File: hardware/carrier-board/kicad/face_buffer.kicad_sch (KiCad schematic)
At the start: 8 parts, among them J2 HUB75, U1 74AHCT245, U2 74AHCT245

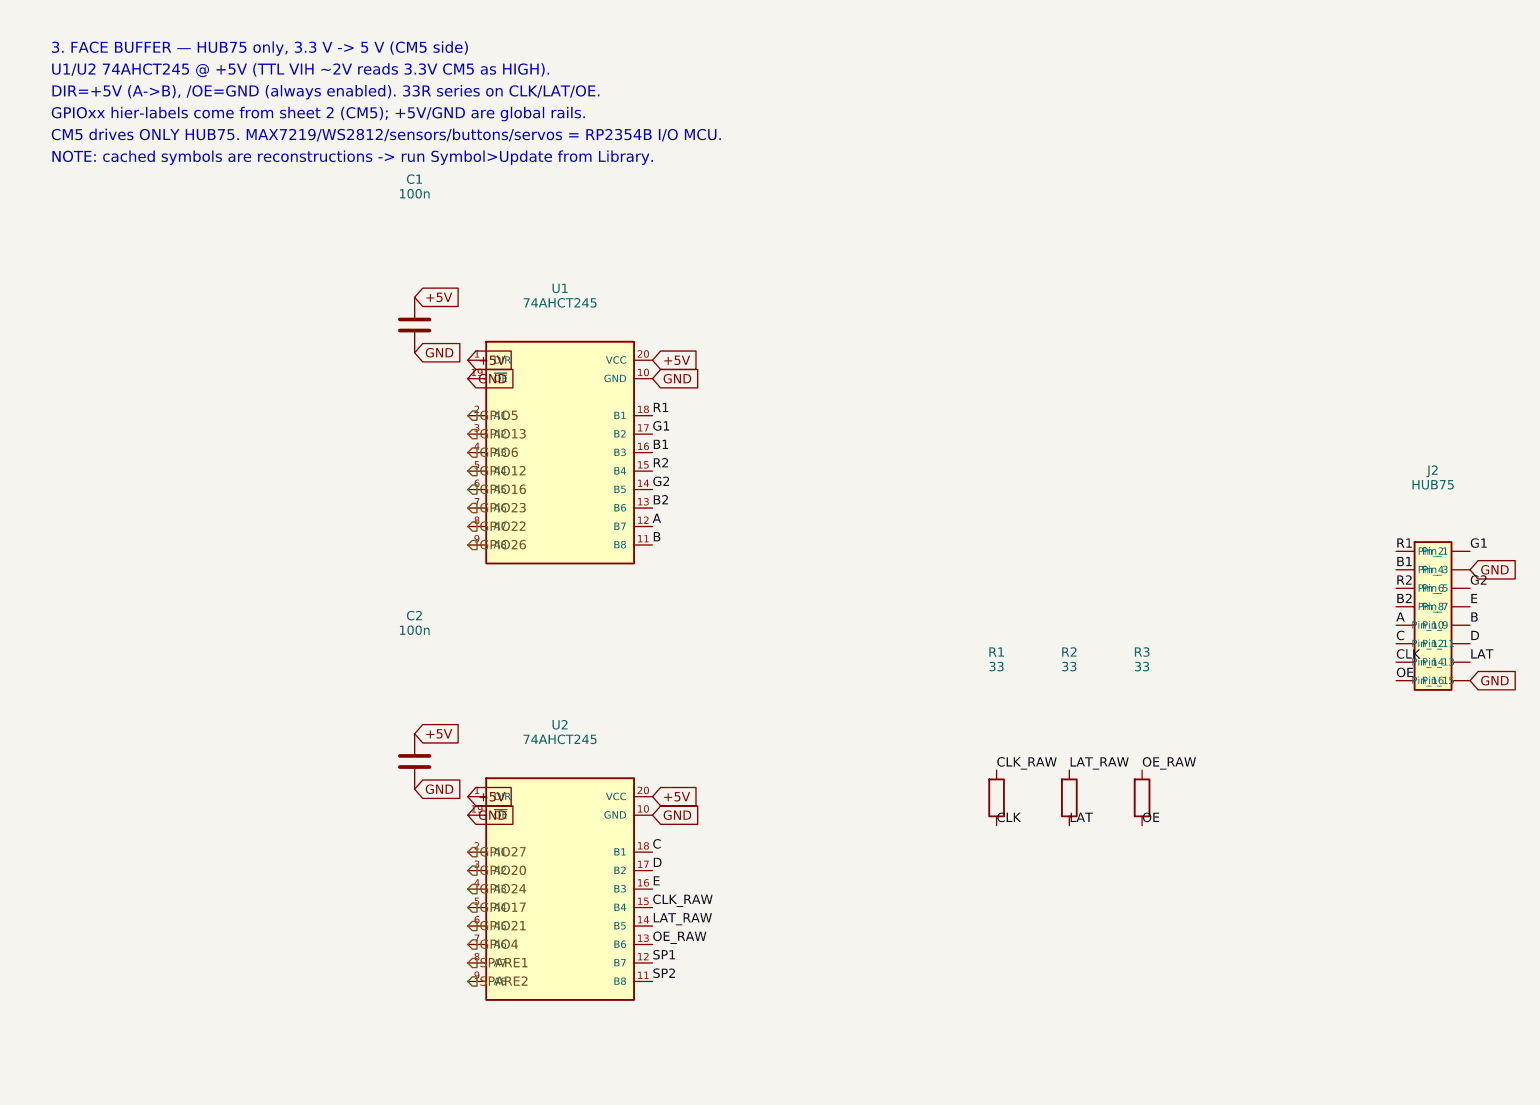
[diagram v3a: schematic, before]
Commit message: Carrier KiCad: populate all 11 schematic sheets
Replace populate_face_buffer.py with populate_sheets.py: one generator that
emits all 11 populated sub-sheets reusing the KiCad-9 format proven by the
face_buffer proof. Shared symbol library + generic box-symbol builder; condensed
CM5 (2x DF40-100) and RP2354B (QFN-80) symbols showing only used pins.

Connectivity by net labels (global for rails + cross-sheet nets: GPIOxx HUB75,
MX_*, LED*_DAT, SRV*, BTN*, *_USB_*; local within-sheet). Sheets: power
(protection + rails + AP2112 +3V3_RP), cm5 (HUB75 out + fan MOSFETs + RP ctrl),
face_buffer, rp2354_io (RP2354B + xtal + SW1/J12 + ESD + SWD), rp2354_face
(U10->J3), leds (U11 quad ->J4a-d), sensors_i2c (pull-ups+J5+STEMMA),
servos (J20-27 + rail), gpio_buttons (J6), usb (USB2514B hub + uplink),
cameras_display (CSI FFC + HDMI).

Verified: all sheets paren-balanced, every used lib_id defined, all instance
paths match sheet UUIDs, root<->sub-sheet UUID linkage intact. generate_skeleton.py
now lists all sheets POPULATED (writes only root+project). Not yet opened in
KiCad here -- expect ERC warnings (PWR_FLAG, unconnected pins) to clean.
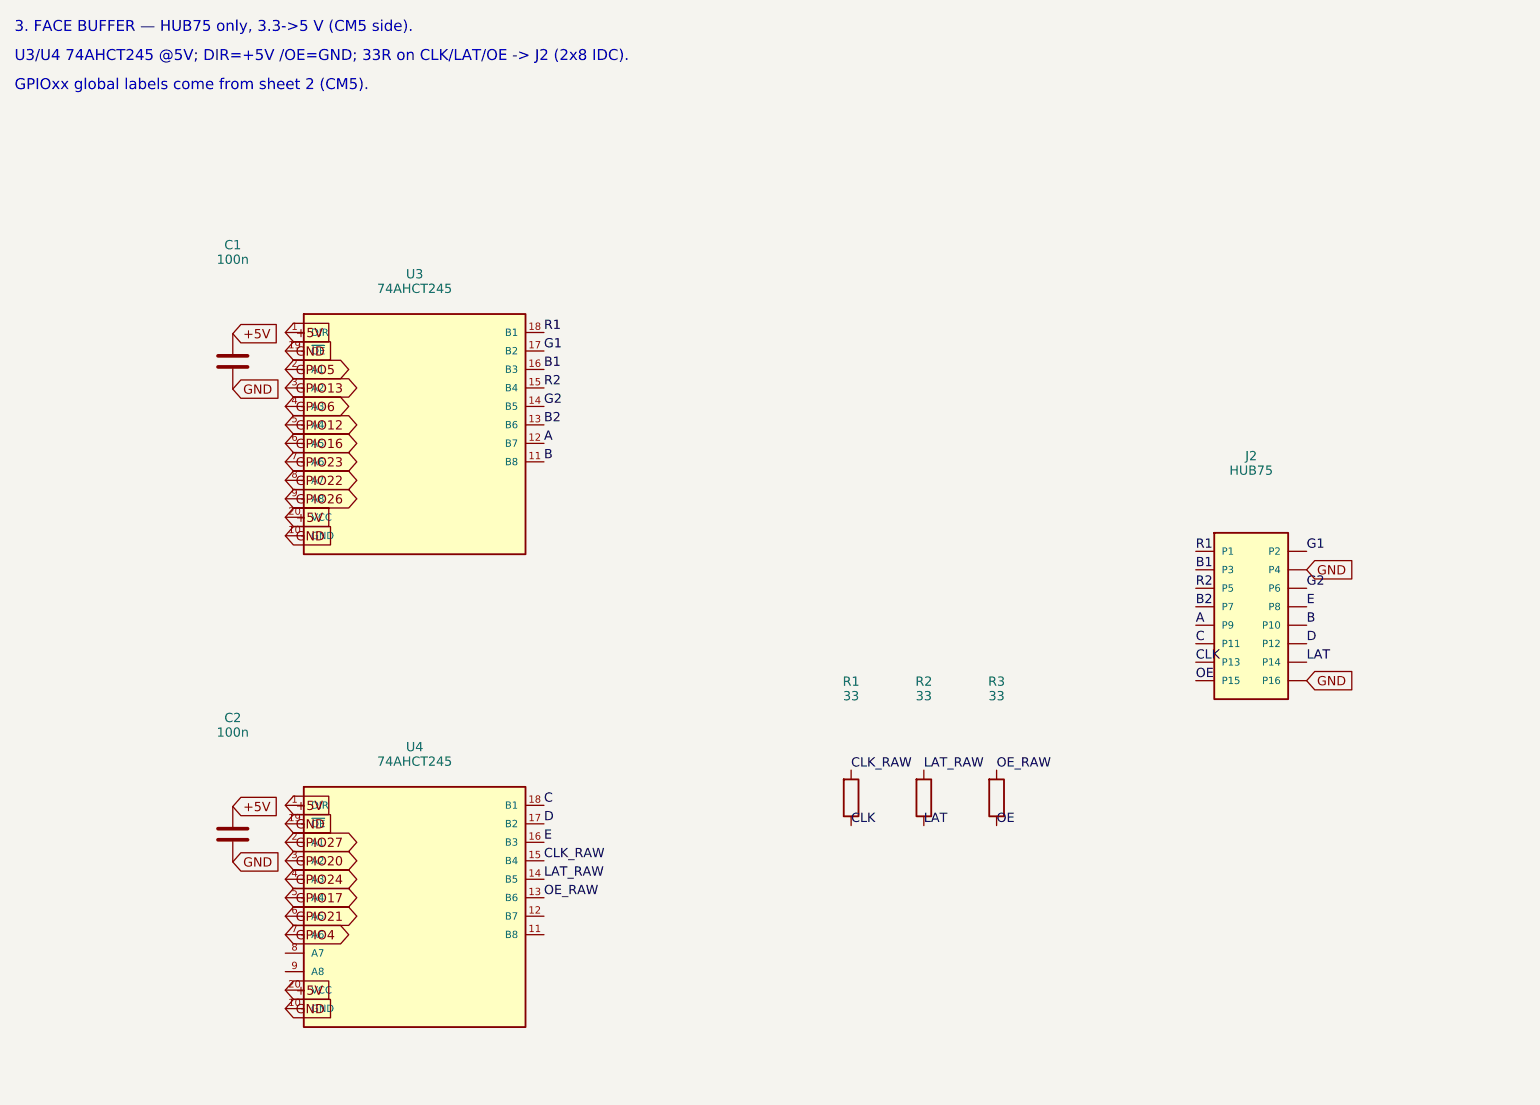
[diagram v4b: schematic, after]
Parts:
- removed U1, U2: 74AHCT245, symbol 74xx:74AHCT245
- added U3, U4: 74AHCT245, symbol 74xx:74AHCT245
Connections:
- net +5V: now also U3.1 (DIR), U3.20 (VCC), U4.1 (DIR), U4.20 (VCC)
- net A: now also U3.12 (B7)
- net B: now also U3.11 (B8)
- net B1: now also U3.16 (B3)
- net B2: now also U3.13 (B6)
- net C: now also U4.18 (B1)
- net CLK_RAW: now also U4.15 (B4)
- net D: now also U4.17 (B2)
- net E: now also U4.16 (B3)
- net G1: now also U3.17 (B2)
- net G2: now also U3.14 (B5)
- net GND: now also U3.10 (GND), U3.19 (~{OE}), U4.10 (GND), U4.19 (~{OE})
- net GPIO12: now also U3.5 (A4)
- net GPIO13: now also U3.3 (A2)
- net GPIO16: now also U3.6 (A5)
- net GPIO17: now also U4.5 (A4)
- net GPIO20: now also U4.3 (A2)
- net GPIO21: now also U4.6 (A5)
- net GPIO22: now also U3.8 (A7)
- net GPIO23: now also U3.7 (A6)
- net GPIO24: now also U4.4 (A3)
- net GPIO26: now also U3.9 (A8)
- net GPIO27: now also U4.2 (A1)
- net GPIO4: now also U4.7 (A6)
- net GPIO5: now also U3.2 (A1)
- net GPIO6: now also U3.4 (A3)
- net LAT_RAW: now also U4.14 (B5)
- net OE_RAW: now also U4.13 (B6)
- net R1: now also U3.18 (B1)
- net R2: now also U3.15 (B4)
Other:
- note added: "3. FACE BUFFER — HUB75 only, 3.3->5 V (CM5 side)."
- note added: "GPIOxx global labels come from sheet 2 (CM5)."
- note added: "U3/U4 74AHCT245 @5V; DIR=+5V /OE=GND; 33R on CLK/LAT/OE -> J2 (2x8 IDC)."
- note removed: "3. FACE BUFFER — HUB75 only, 3.3 V -> 5 V (CM5 side)"
- note removed: "CM5 drives ONLY HUB75. MAX7219/WS2812/sensors/buttons/servos = RP2354B I/O MCU."
- note removed: "DIR=+5V (A->B), /OE=GND (always enabled). 33R series on CLK/LAT/OE."
- note removed: "GPIOxx hier-labels come from sheet 2 (CM5); +5V/GND are global rails."
- note removed: "NOTE: cached symbols are reconstructions -> run Symbol>Update from Library."
- note removed: "U1/U2 74AHCT245 @ +5V (TTL VIH ~2V reads 3.3V CM5 as HIGH)."
